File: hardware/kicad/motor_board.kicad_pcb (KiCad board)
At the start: 2 copper layers, 81 parts, among them IC1 TLE52062GAUMA1, IC2 TLE52062GAUMA1, IC3 TLE52062GAUMA1, IC4 LM3940IMP-3.3, J1 MOT1, J10 ENC8, J11 SWD, J12 SPI, J13 CAN, J2 MOT2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

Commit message: Finish PCBV0.1
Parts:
- added D2: PMEG2010EB, _Diodes_GRZ:PMEG2010EB, F.Cu at (178.2, 105.0)
- added D3: PMEG2010EB, _Diodes_GRZ:PMEG2010EB, F.Cu at (185.4, 88.5)
- added G***: RustyDucks, myFootprints:RustyDuck, B.Cu at (137.0, 107.6)
- added P1: Power_pads, myFootprints:Power_pads, F.Cu at (185.2, 143.8)
- added REF**: MountingHole_5mm, MountingHole:MountingHole_5mm, F.Cu at (189.0, 45.0)
- added REF**: MountingHole_3mm, MountingHole:MountingHole_3mm, F.Cu at (109.0, 151.0)
- added REF**: MountingHole_3mm, MountingHole:MountingHole_3mm, F.Cu at (189.0, 151.0)
- added REF**: MountingHole_3mm, MountingHole:MountingHole_3mm, F.Cu at (189.0, 75.0)
- added REF**: MountingHole_3mm, MountingHole:MountingHole_3mm, F.Cu at (109.0, 75.0)
- added REF**: MountingHole_5mm, MountingHole:MountingHole_5mm, F.Cu at (109.0, 45.0)
- moved R4 52.6 mm to (156.2, 95.6), turned to 180 degrees
- moved R5 52.3 mm to (157.1, 93.6), turned to 180 degrees
- moved JP1 51.4 mm to (182.0, 105.0), turned to 180 degrees
- moved C11 46.5 mm to (180.5, 110.6)
- moved C1 45.1 mm to (176.9, 146.2), turned to 270 degrees
- moved C2 40.5 mm to (173.1, 146.5), turned to 90 degrees
- moved L1 40.4 mm to (182.2, 122.2), turned to 180 degrees
- moved J6 39.1 mm to (190.5, 86.4), turned to 90 degrees
- moved IC4 38.1 mm to (181.9, 98.0)
- moved C3 35.3 mm to (175.9, 136.9), turned to 270 degrees
- moved C12 34.7 mm to (187.2, 108.0), turned to 90 degrees
- moved R2 31.7 mm to (187.1, 113.6), turned to 270 degrees
- moved C20 31.2 mm to (181.7, 93.5)
- moved R3 30.8 mm to (188.6, 113.6), turned to 90 degrees
- moved C24 30.6 mm to (181.7, 102.4)
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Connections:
- J7 pad 4: /ENC2B -> /ENC2A
- J7 pad 5: /ENC2A -> /ENC2B
- JP1 pad 2: +5V -> Net-(D2-Pad2)
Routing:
- net GND: track 179.0 -> 737.1 mm, vias 0 -> 7
- net +3V3: track 39.2 -> 355.2 mm, vias 0 -> 10
- net +5V: track 6.50 -> 182.2 mm, vias 0 -> 2
- net /USB_DM: track 0.00 -> 47.6 mm, vias 0 -> 4
- net /USB_DP: track 0.00 -> 46.7 mm, vias 0 -> 4
- net /LED_CAN: track 0.00 -> 44.0 mm, vias 0 -> 2
- net VBAT: track 156.1 -> 198.1 mm
- net /USB_VBUS: track 0.00 -> 41.3 mm, vias 0 -> 2
- net Net-(C11-Pad1): track 0.00 -> 36.6 mm
- net Net-(R2-Pad2): track 0.00 -> 23.9 mm
- net Net-(R4-Pad1): track 0.00 -> 23.8 mm, vias 0 -> 2
- net Net-(C10-Pad2): track 0.00 -> 19.8 mm
- net Net-(LED3-Pad2): track 18.6 -> 1.87 mm
- net /LED4: track 6.48 -> 23.2 mm
- net Net-(LED4-Pad2): track 18.1 -> 1.87 mm
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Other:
- board outline added: 86 x 82 mm
- board text added: "A"
- board text added: "B"
- board text added: "C"
- board text added: "CAN"
- board text added: "D"
- board text added: "Encoder 1"
- board text added: "Encoder 2"
- board text added: "Encoder 3"
- board text added: "Encoder 4"
- board text added: "I2C"
- board text added: "MOT1"
- board text added: "MOT2"
- board text added: "MOT3"
- board text added: "Motor Board V0.1"
- board text added: "SPI"
- board text added: "SWD"
- board text added: "The Rusty Ducks"
- board text added: "UART"

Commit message: Edit for Stencil
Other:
- board size 86 x 82 mm -> 126 x 178 mm
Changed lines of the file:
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@@
     (thickness 1.6)
     (drawings 25)
-    (tracks 989)
+    (tracks 990)
     (zones 0)
     (modules 91)
@@
   )
   (setup
-    (last_trace_width 0.4)
+    (last_trace_width 0.25)
     (user_trace_width 0.127)
     (user_trace_width 0.2)
@@
     (mod_text_size 1 1)
     (mod_text_width 0.15)
-    (pad_size 1.524 1.524)
-    (pad_drill 0.762)
+    (pad_size 5 5)
+    (pad_drill 5)
     (pad_to_mask_clearance 0.051)
     (solder_mask_min_width 0.25)
@@
       (outputformat 1)
       (mirror false)
-      (drillshape 1)
+      (drillshape 0)
       (scaleselection 1)
-      (outputdirectory ""))
+      (outputdirectory "stencil/"))
   )
   (net 0 "")
@@
     (fp_circle (center 0 0) (end 5 0) (layer Cmts.User) (width 0.15))
     (fp_circle (center 0 0) (end 5.25 0) (layer F.CrtYd) (width 0.05))
-    (pad 1 np_thru_hole circle (at 0 0) (size 5 5) (drill 5) (layers *.Cu *.Mask))
+    (pad "" np_thru_hole circle (at 0 0) (size 5 5) (drill 5) (layers *.Cu F.Paste))
   )
   (module MountingHole:MountingHole_3mm (layer F.Cu)
@@
       (effects (font (size 1 1) (thickness 0.15)))
     )
-    (pad 1 np_thru_hole circle (at 0 0) (size 5 5) (drill 5) (layers *.Cu *.Mask))
+    (pad "" np_thru_hole circle (at 0 0) (size 5 5) (drill 5) (layers *.Cu F.Paste))
   )
-  (gr_line (start 106 72) (end 192 72) (layer Edge.Cuts) (width 0.05))
+  (gr_line (start 86 26) (end 212 26) (layer Edge.Cuts) (width 0.05))
   (gr_text "Motor Board V0.1" (at 169.545 122.301) (layer B.SilkS)
     (effects (font (size 3 3) (thickness 0.5)) (justify mirror))
@@
   (gr_circle (center 182.88 130.302) (end 182.626 130.556) (layer F.SilkS) (width 0.2))
   (gr_circle (center 140.716 85.598) (end 140.97 85.852) (layer F.SilkS) (width 0.2))
-  (gr_line (start 106 72) (end 106 154) (layer Edge.Cuts) (width 0.05))
-  (gr_line (start 192 154) (end 106 154) (layer Edge.Cuts) (width 0.05))
-  (gr_line (start 192 72) (end 192 154) (layer Edge.Cuts) (width 0.05))
+  (gr_line (start 86 26) (end 86 204) (layer Edge.Cuts) (width 0.05))
+  (gr_line (start 212 204) (end 86 204) (layer Edge.Cuts) (width 0.05))
+  (gr_line (start 212 26) (end 212 204) (layer Edge.Cuts) (width 0.05))
   (segment (start 127 140.665) (end 126.06 141.605) (width 0.5) (layer F.Cu) (net 1))
   (segment (start 127 136.15) (end 127 140.665) (width 0.5) (layer F.Cu) (net 1))
@@
   (segment (start 123.152 90.551) (end 121.285 90.551) (width 0.4) (layer F.Cu) (net 52))
   (segment (start 122.771 95.123) (end 121.285 95.123) (width 0.4) (layer F.Cu) (net 53))
+  (segment (start 122.771 95.123) (end 123.152 95.123) (width 0.4) (layer F.Cu) (net 53))
   (segment (start 123.152 104.521) (end 121.285 104.521) (width 0.4) (layer F.Cu) (net 54))
   (segment (start 123.152 99.949) (end 121.285 99.949) (width 0.4) (layer F.Cu) (net 55))

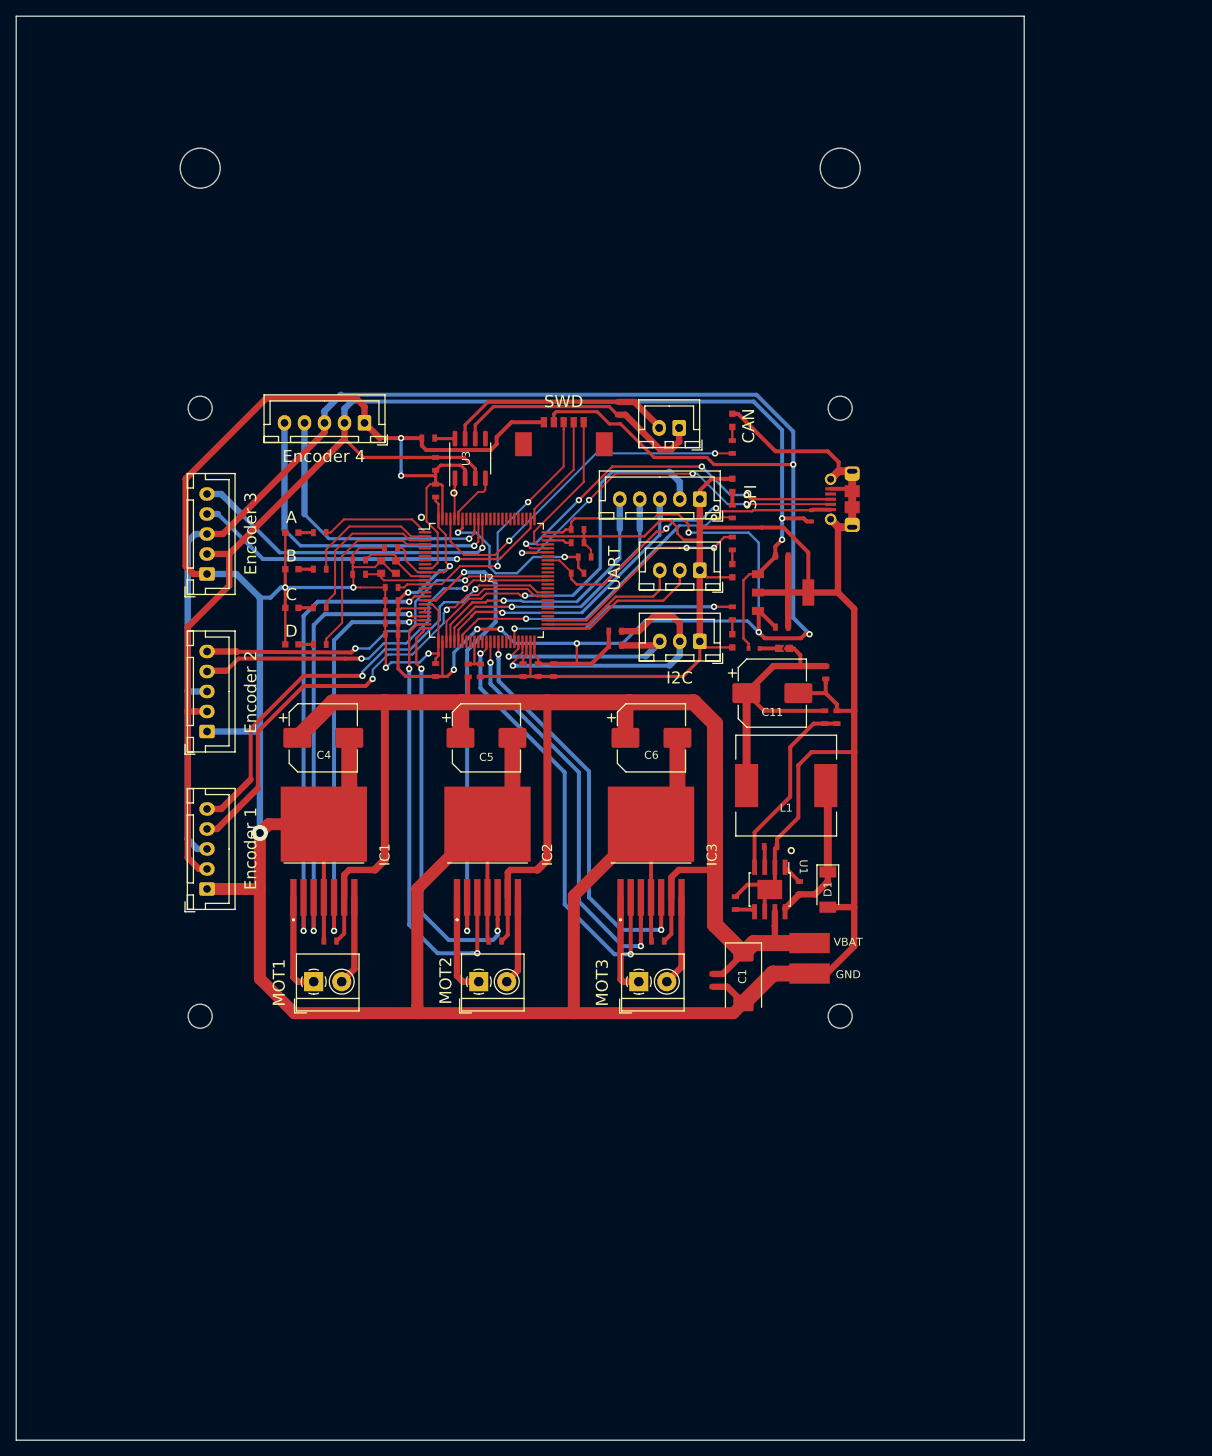
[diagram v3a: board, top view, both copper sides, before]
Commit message: Back to original size (no stencil)
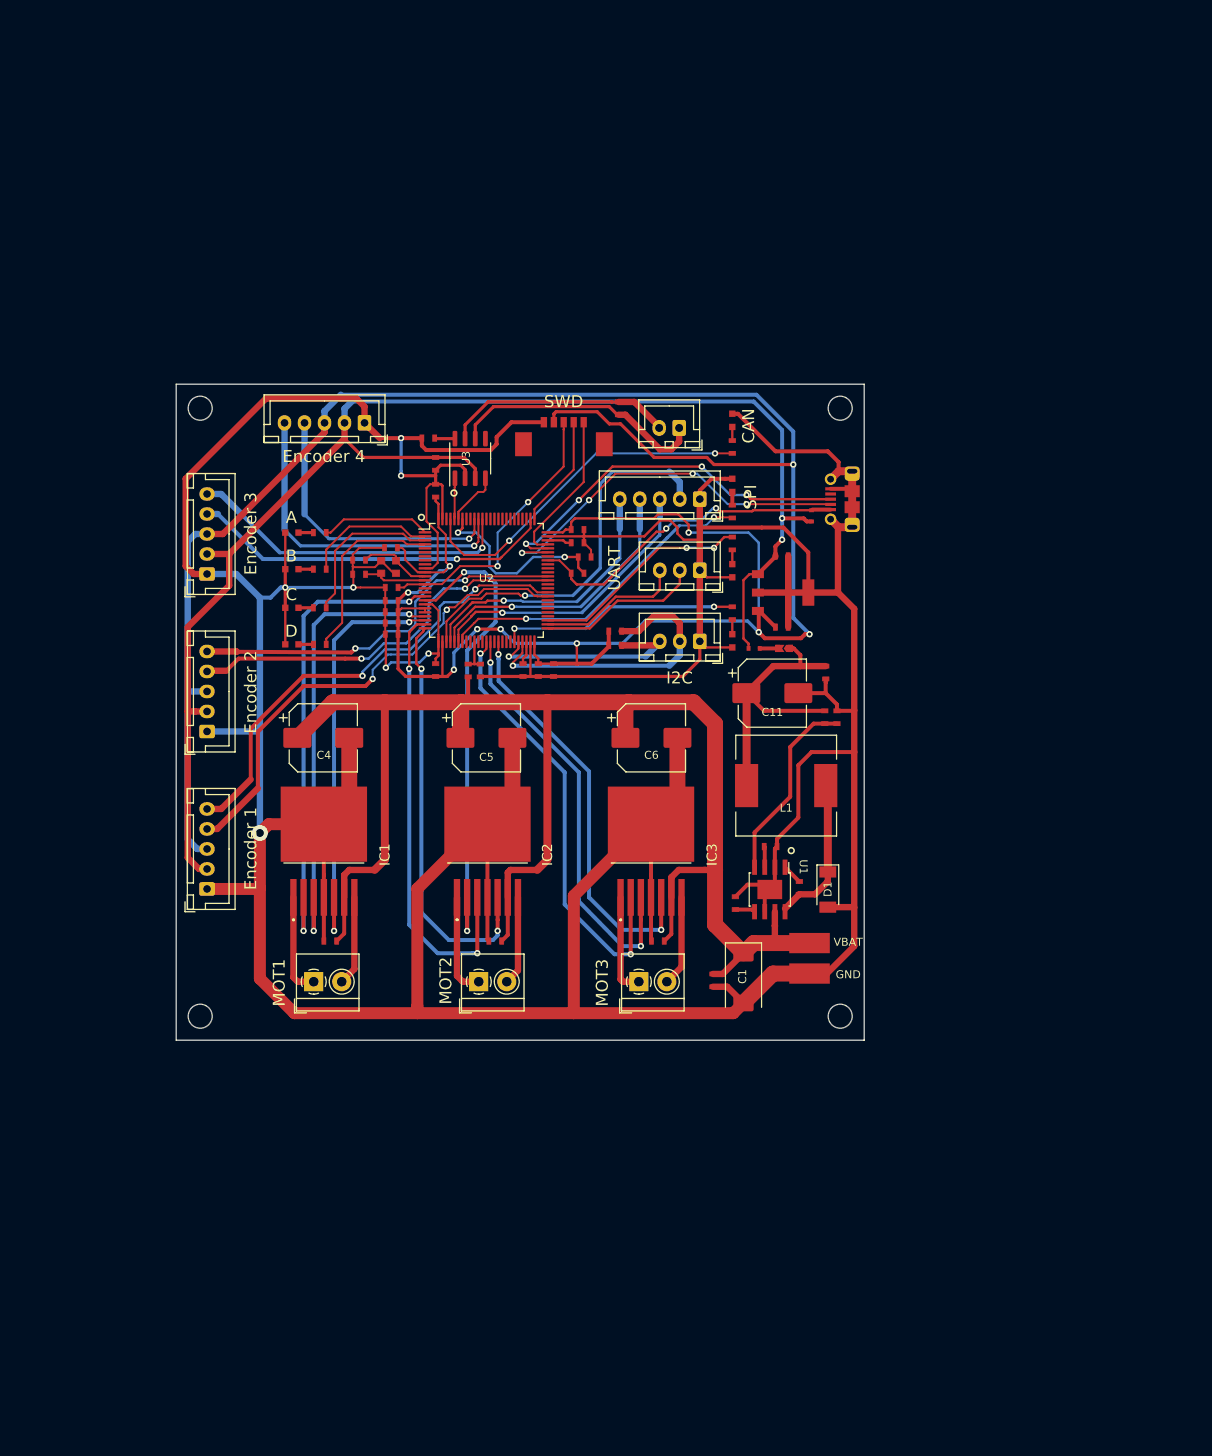
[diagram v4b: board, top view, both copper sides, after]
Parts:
- removed the REF** at (189.0, 45.0)
- removed the REF** at (109.0, 45.0)
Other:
- board size 126 x 178 mm -> 86 x 82 mm
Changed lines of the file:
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@@
     (tracks 990)
     (zones 0)
-    (modules 91)
+    (modules 89)
     (nets 118)
   )
@@
     (add_net VBAT)
   )
-  (module MountingHole:MountingHole_5mm (layer F.Cu)
-    (at 189 45)
-    (descr "Mounting Hole 5mm, no annular")
-    (tags "mounting hole 5mm no annular")
-    (attr virtual)
-    (fp_text reference REF** (at 0 -6) (layer F.SilkS) hide
-      (effects (font (size 1 1) (thickness 0.15)))
-    )
-    (fp_text value MountingHole_5mm (at 0 6) (layer F.Fab) hide
-      (effects (font (size 1 1) (thickness 0.15)))
-    )
-    (fp_text user %R (at 0.3 0) (layer F.Fab)
-      (effects (font (size 1 1) (thickness 0.15)))
-    )
-    (fp_circle (center 0 0) (end 5 0) (layer Cmts.User) (width 0.15))
-    (fp_circle (center 0 0) (end 5.25 0) (layer F.CrtYd) (width 0.05))
-    (pad "" np_thru_hole circle (at 0 0) (size 5 5) (drill 5) (layers *.Cu F.Paste))
-  )
   (module MountingHole:MountingHole_3mm (layer F.Cu)
     (at 109 151)
@@
       (xy 0.71152 -7.941031) (xy 0.791473 -7.874859) (xy 0.800121 -7.874) (xy 0.884438 -7.909697)) (layer B.SilkS) (width 0.01))
   )
-  (module MountingHole:MountingHole_5mm (layer F.Cu)
-    (at 109 45)
-    (descr "Mounting Hole 5mm, no annular")
-    (tags "mounting hole 5mm no annular")
-    (attr virtual)
-    (fp_text reference REF** (at 0 -6) (layer F.SilkS) hide
-      (effects (font (size 1 1) (thickness 0.15)))
-    )
-    (fp_text value MountingHole_5mm (at 0 6) (layer F.Fab) hide
-      (effects (font (size 1 1) (thickness 0.15)))
-    )
-    (fp_circle (center 0 0) (end 5.25 0) (layer F.CrtYd) (width 0.05))
-    (fp_circle (center 0 0) (end 5 0) (layer Cmts.User) (width 0.15))
-    (fp_text user %R (at 0.3 0) (layer F.Fab)
-      (effects (font (size 1 1) (thickness 0.15)))
-    )
-    (pad "" np_thru_hole circle (at 0 0) (size 5 5) (drill 5) (layers *.Cu F.Paste))
-  )
-  (gr_line (start 86 26) (end 212 26) (layer Edge.Cuts) (width 0.05))
+  (gr_line (start 106 72) (end 192 72) (layer Edge.Cuts) (width 0.05))
   (gr_text "Motor Board V0.1" (at 169.545 122.301) (layer B.SilkS)
     (effects (font (size 3 3) (thickness 0.5)) (justify mirror))
@@
   (gr_circle (center 182.88 130.302) (end 182.626 130.556) (layer F.SilkS) (width 0.2))
   (gr_circle (center 140.716 85.598) (end 140.97 85.852) (layer F.SilkS) (width 0.2))
-  (gr_line (start 86 26) (end 86 204) (layer Edge.Cuts) (width 0.05))
-  (gr_line (start 212 204) (end 86 204) (layer Edge.Cuts) (width 0.05))
-  (gr_line (start 212 26) (end 212 204) (layer Edge.Cuts) (width 0.05))
+  (gr_line (start 106 72) (end 106 154) (layer Edge.Cuts) (width 0.05))
+  (gr_line (start 192 154) (end 106 154) (layer Edge.Cuts) (width 0.05))
+  (gr_line (start 192 72) (end 192 154) (layer Edge.Cuts) (width 0.05))
   (segment (start 127 140.665) (end 126.06 141.605) (width 0.5) (layer F.Cu) (net 1))
   (segment (start 127 136.15) (end 127 140.665) (width 0.5) (layer F.Cu) (net 1))
